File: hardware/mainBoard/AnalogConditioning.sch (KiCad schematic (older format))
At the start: 23 parts

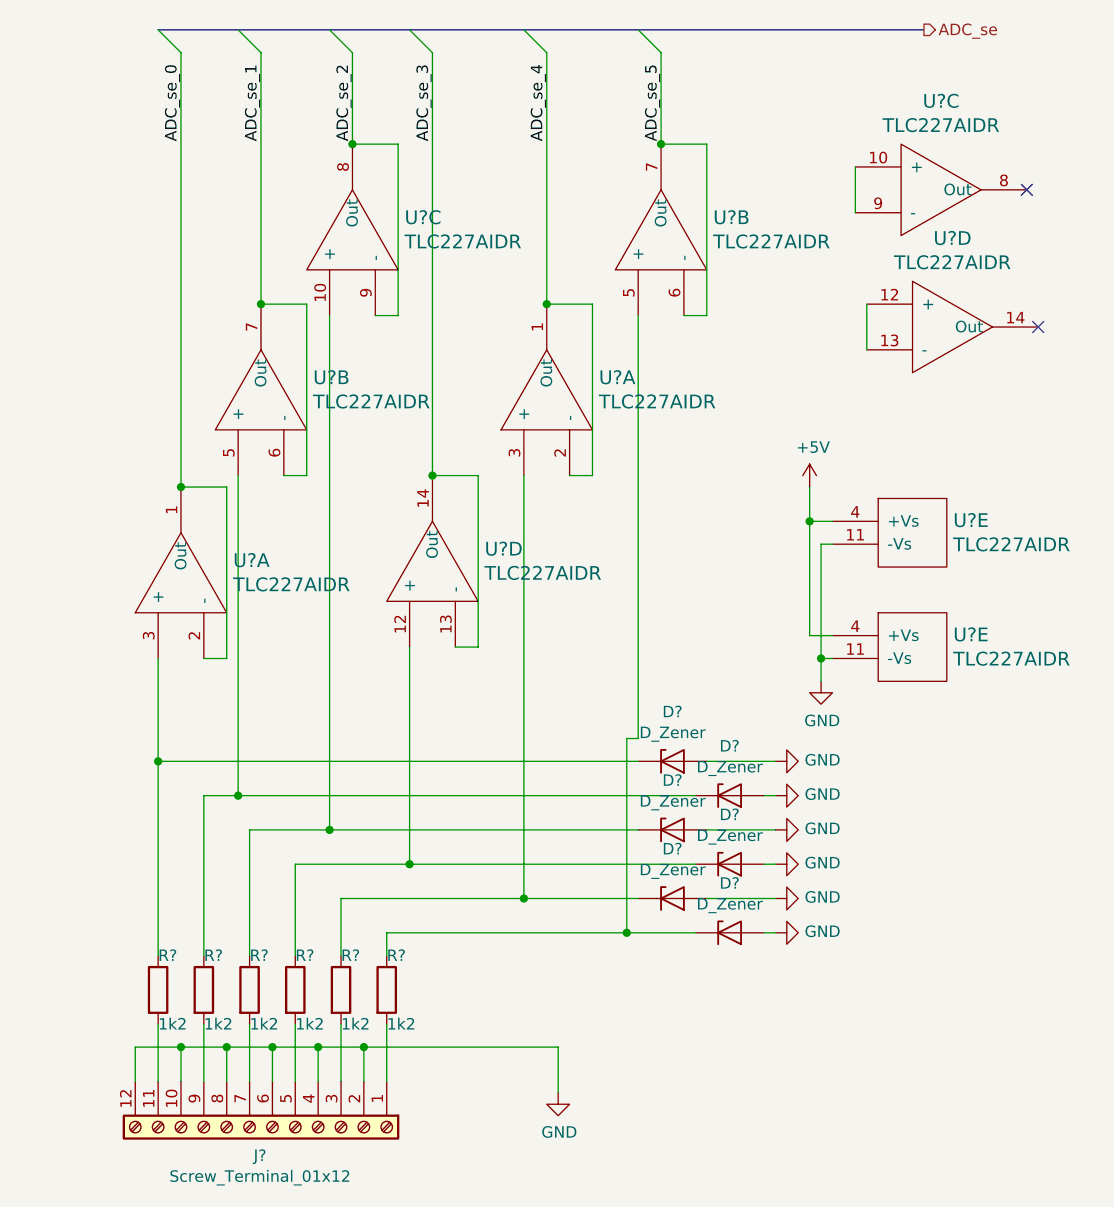
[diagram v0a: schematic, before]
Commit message: Ended schematic, created some pcb footprints
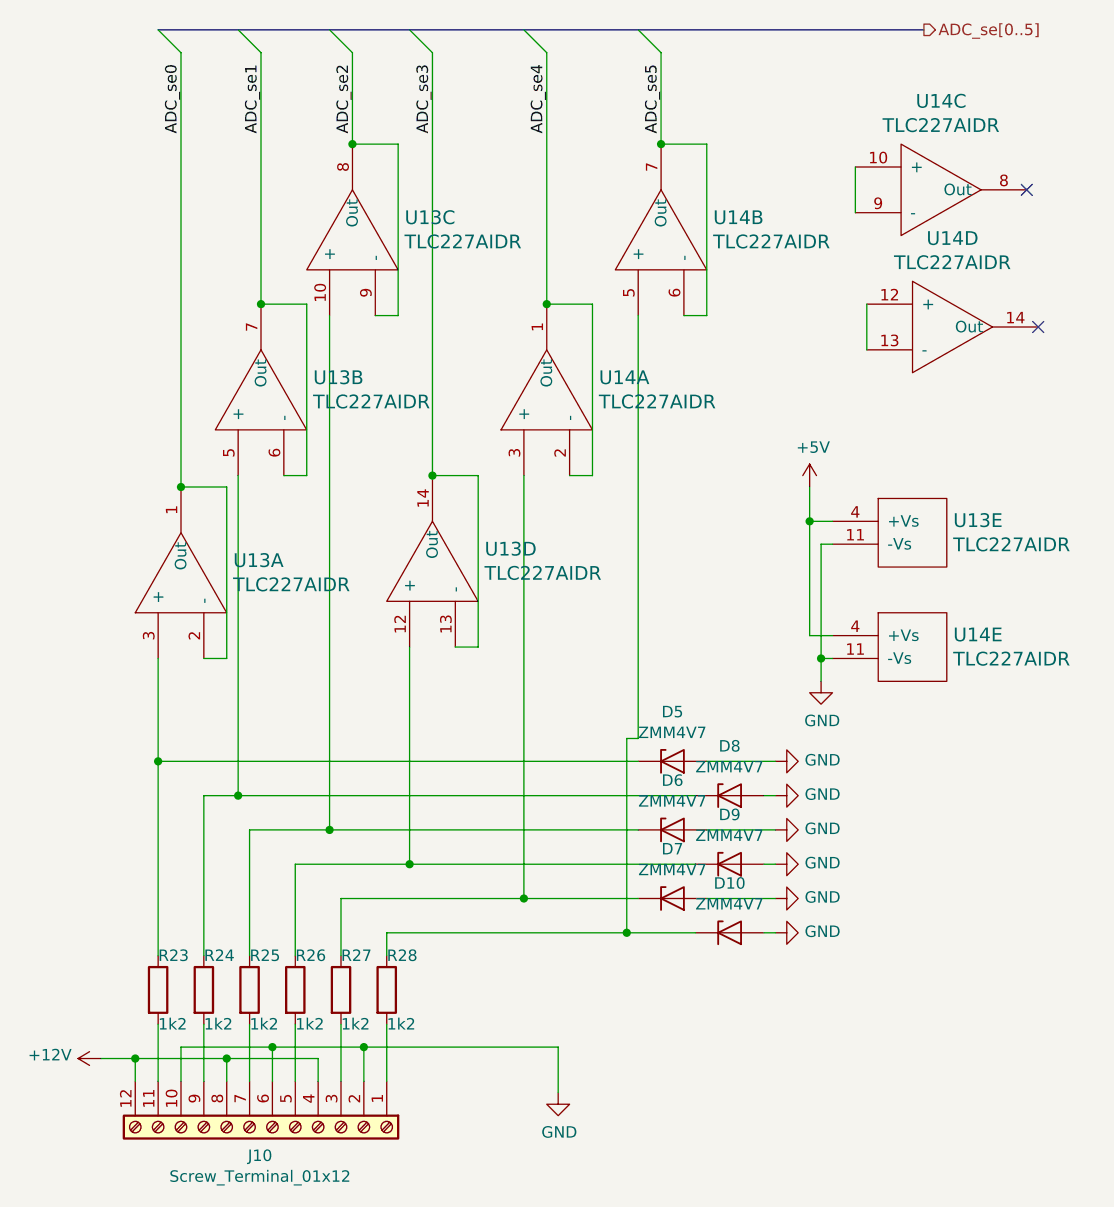
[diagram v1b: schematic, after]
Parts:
- D10, D5, D6, D7, D8, D9: renamed from D?; value D_Zener -> ZMM4V7; footprint (none) -> Diode_SMD:D_MiniMELF
- J10: renamed from J?; footprint (none) -> chinalandfoot:TerminalBlock_12_P5.08mm
- R23, R24, R25, R26, R27, R28: renamed from R?; footprint (none) -> Resistor_SMD:R_0603_1608Metric_Pad1.05x0.95mm_HandSolder
- U13, U14: renamed from U?; footprint (none) -> Package_SO:SOIC-14_3.9x8.7mm_P1.27mm
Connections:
- net GND: no longer J10.12 (Pin_12), J10.4 (Pin_4), J10.8 (Pin_8)
- net ADC_se_0 renamed ADC_se0
- net ADC_se_1 renamed ADC_se1
- net ADC_se_2 renamed ADC_se2
- net ADC_se_3 renamed ADC_se3
- net ADC_se_4 renamed ADC_se4
- net ADC_se_5 renamed ADC_se5
- new net +12V: J10.12 (Pin_12), J10.4 (Pin_4), J10.8 (Pin_8)

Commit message: First working software
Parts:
- D10, D5, D6, D7, D8, D9: URL (none) -> https://lcsc.com/product-detail/Zener-Diodes_ST-Semtech-ZMM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
- R23, R24, R25, R26, R27, R28: URL (none) -> https://lcsc.com/product-detail/Chip-Resistor-Surface-Mount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
- U13, U14: URL (none) -> https://lcsc.com/product-detail/Precision-OpAmps_Texas-Inst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
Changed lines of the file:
@@
 EESchema Schematic File Version 4
+LIBS:prockeckv2-cache
 EELAYER 30 0
 EELAYER END
@@
 F 2 "Resistor_SMD:R_0603_1608Metric_Pad1.05x0.95mm_HandSolder" V 3580 5450 50  0001 C CNN
 F 3 "~" H 3650 5450 50  0001 C CNN
+F 4 "https://lcsc.com/product-detail/Chip-Resistor-Surface-Mount_UNI-ROYAL-Uniroyal-Elec-0603WAJ0122T5E_C25987.html" H 3650 5450 50  0001 C CNN "URL"
 	1    3650 5450
 	1    0    0    -1
@@
 F 2 "Resistor_SMD:R_0603_1608Metric_Pad1.05x0.95mm_HandSolder" V 3780 5450 50  0001 C CNN
 F 3 "~" H 3850 5450 50  0001 C CNN
+F 4 "https://lcsc.com/product-detail/Chip-Resistor-Surface-Mount_UNI-ROYAL-Uniroyal-Elec-0603WAJ0122T5E_C25987.html" H 3850 5450 50  0001 C CNN "URL"
 	1    3850 5450
 	1    0    0    -1
@@
 F 2 "Resistor_SMD:R_0603_1608Metric_Pad1.05x0.95mm_HandSolder" V 3980 5450 50  0001 C CNN
 F 3 "~" H 4050 5450 50  0001 C CNN
+F 4 "https://lcsc.com/product-detail/Chip-Resistor-Surface-Mount_UNI-ROYAL-Uniroyal-Elec-0603WAJ0122T5E_C25987.html" H 4050 5450 50  0001 C CNN "URL"
 	1    4050 5450
 	1    0    0    -1
@@
 F 2 "Resistor_SMD:R_0603_1608Metric_Pad1.05x0.95mm_HandSolder" V 4180 5450 50  0001 C CNN
 F 3 "~" H 4250 5450 50  0001 C CNN
+F 4 "https://lcsc.com/product-detail/Chip-Resistor-Surface-Mount_UNI-ROYAL-Uniroyal-Elec-0603WAJ0122T5E_C25987.html" H 4250 5450 50  0001 C CNN "URL"
 	1    4250 5450
 	1    0    0    -1
@@
 F 2 "Resistor_SMD:R_0603_1608Metric_Pad1.05x0.95mm_HandSolder" V 4380 5450 50  0001 C CNN
 F 3 "~" H 4450 5450 50  0001 C CNN
+F 4 "https://lcsc.com/product-detail/Chip-Resistor-Surface-Mount_UNI-ROYAL-Uniroyal-Elec-0603WAJ0122T5E_C25987.html" H 4450 5450 50  0001 C CNN "URL"
 	1    4450 5450
 	1    0    0    -1
@@
 F 2 "Resistor_SMD:R_0603_1608Metric_Pad1.05x0.95mm_HandSolder" V 4580 5450 50  0001 C CNN
 F 3 "~" H 4650 5450 50  0001 C CNN
+F 4 "https://lcsc.com/product-detail/Chip-Resistor-Surface-Mount_UNI-ROYAL-Uniroyal-Elec-0603WAJ0122T5E_C25987.html" H 4650 5450 50  0001 C CNN "URL"
 	1    4650 5450
 	1    0    0    -1
@@
 F 2 "Diode_SMD:D_MiniMELF" H 6150 5200 50  0001 C CNN
 F 3 "~" H 6150 5200 50  0001 C CNN
+F 4 "https://lcsc.com/product-detail/Zener-Diodes_ST-Semtech-ZMM4V7_C8060.html" H 6150 5200 50  0001 C CNN "URL"
 	1    6150 5200
 	1    0    0    -1
@@
 F 2 "Diode_SMD:D_MiniMELF" H 5900 5050 50  0001 C CNN
 F 3 "~" H 5900 5050 50  0001 C CNN
+F 4 "https://lcsc.com/product-detail/Zener-Diodes_ST-Semtech-ZMM4V7_C8060.html" H 5900 5050 50  0001 C CNN "URL"
 	1    5900 5050
 	1    0    0    -1
@@
 F 2 "Diode_SMD:D_MiniMELF" H 6150 4900 50  0001 C CNN
 F 3 "~" H 6150 4900 50  0001 C CNN
+F 4 "https://lcsc.com/product-detail/Zener-Diodes_ST-Semtech-ZMM4V7_C8060.html" H 6150 4900 50  0001 C CNN "URL"
 	1    6150 4900
 	1    0    0    -1
@@
 F 2 "Diode_SMD:D_MiniMELF" H 5900 4750 50  0001 C CNN
 F 3 "~" H 5900 4750 50  0001 C CNN
+F 4 "https://lcsc.com/product-detail/Zener-Diodes_ST-Semtech-ZMM4V7_C8060.html" H 5900 4750 50  0001 C CNN "URL"
 	1    5900 4750
 	1    0    0    -1
@@
 F 2 "Diode_SMD:D_MiniMELF" H 6150 4600 50  0001 C CNN
 F 3 "~" H 6150 4600 50  0001 C CNN
+F 4 "https://lcsc.com/product-detail/Zener-Diodes_ST-Semtech-ZMM4V7_C8060.html" H 6150 4600 50  0001 C CNN "URL"
 	1    6150 4600
 	1    0    0    -1
@@
 F 2 "Diode_SMD:D_MiniMELF" H 5900 4450 50  0001 C CNN
 F 3 "~" H 5900 4450 50  0001 C CNN
+F 4 "https://lcsc.com/product-detail/Zener-Diodes_ST-Semtech-ZMM4V7_C8060.html" H 5900 4450 50  0001 C CNN "URL"
 	1    5900 4450
 	1    0    0    -1
@@
 F 2 "Package_SO:SOIC-14_3.9x8.7mm_P1.27mm" H 7050 3500 60  0001 C CNN
 F 3 "" H 7050 3500 60  0001 C CNN
+F 4 "https://lcsc.com/product-detail/Precision-OpAmps_Texas-Instruments-TLC2274AIDR_C93026.html" H 6950 3450 50  0001 C CNN "URL"
 	5    6950 3450
 	1    0    0    -1
@@
 F 2 "Package_SO:SOIC-14_3.9x8.7mm_P1.27mm" H 4200 2850 60  0001 C CNN
 F 3 "" H 4200 2850 60  0001 C CNN
+F 4 "https://lcsc.com/product-detail/Precision-OpAmps_Texas-Instruments-TLC2274AIDR_C93026.html" H 4100 2800 50  0001 C CNN "URL"
 	2    4100 2800
 	0    -1   -1   0
@@
 F 2 "Package_SO:SOIC-14_3.9x8.7mm_P1.27mm" H 4600 2150 60  0001 C CNN
 F 3 "" H 4600 2150 60  0001 C CNN
+F 4 "https://lcsc.com/product-detail/Precision-OpAmps_Texas-Instruments-TLC2274AIDR_C93026.html" H 4500 2100 50  0001 C CNN "URL"
 	3    4500 2100
 	0    -1   -1   0
@@
 F 2 "Package_SO:SOIC-14_3.9x8.7mm_P1.27mm" H 4950 3600 60  0001 C CNN
 F 3 "" H 4950 3600 60  0001 C CNN
+F 4 "https://lcsc.com/product-detail/Precision-OpAmps_Texas-Instruments-TLC2274AIDR_C93026.html" H 4850 3550 50  0001 C CNN "URL"
 	4    4850 3550
 	0    -1   -1   0
@@
 F 2 "Package_SO:SOIC-14_3.9x8.7mm_P1.27mm" H 5450 2850 60  0001 C CNN
 F 3 "" H 5450 2850 60  0001 C CNN
+F 4 "https://lcsc.com/product-detail/Precision-OpAmps_Texas-Instruments-TLC2274AIDR_C93026.html" H 5350 2800 50  0001 C CNN "URL"
 	1    5350 2800
 	0    -1   -1   0
@@
 F 2 "Package_SO:SOIC-14_3.9x8.7mm_P1.27mm" H 7200 2000 60  0001 C CNN
 F 3 "" H 7200 2000 60  0001 C CNN
+F 4 "https://lcsc.com/product-detail/Precision-OpAmps_Texas-Instruments-TLC2274AIDR_C93026.html" H 7100 1950 50  0001 C CNN "URL"
 	3    7100 1950
 	1    0    0    -1
@@
 F 2 "Package_SO:SOIC-14_3.9x8.7mm_P1.27mm" H 7250 2600 60  0001 C CNN
 F 3 "" H 7250 2600 60  0001 C CNN
+F 4 "https://lcsc.com/product-detail/Precision-OpAmps_Texas-Instruments-TLC2274AIDR_C93026.html" H 7150 2550 50  0001 C CNN "URL"
 	4    7150 2550
 	1    0    0    -1
@@
 F 2 "Package_SO:SOIC-14_3.9x8.7mm_P1.27mm" H 7050 4000 60  0001 C CNN
 F 3 "" H 7050 4000 60  0001 C CNN
+F 4 "https://lcsc.com/product-detail/Precision-OpAmps_Texas-Instruments-TLC2274AIDR_C93026.html" H 6950 3950 50  0001 C CNN "URL"
 	5    6950 3950
 	1    0    0    -1
@@
 F 2 "Package_SO:SOIC-14_3.9x8.7mm_P1.27mm" H 5950 2150 60  0001 C CNN
 F 3 "" H 5950 2150 60  0001 C CNN
+F 4 "https://lcsc.com/product-detail/Precision-OpAmps_Texas-Instruments-TLC2274AIDR_C93026.html" H 5850 2100 50  0001 C CNN "URL"
 	2    5850 2100
 	0    -1   -1   0
@@
 F 2 "Package_SO:SOIC-14_3.9x8.7mm_P1.27mm" H 3850 3650 60  0001 C CNN
 F 3 "" H 3850 3650 60  0001 C CNN
+F 4 "https://lcsc.com/product-detail/Precision-OpAmps_Texas-Instruments-TLC2274AIDR_C93026.html" H 3750 3600 50  0001 C CNN "URL"
 	1    3750 3600
 	0    -1   -1   0
